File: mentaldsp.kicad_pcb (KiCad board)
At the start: 2 copper layers, 90 x 70 mm, 10 parts, among them J1 NEMA Conn, J2 NEMA Conn, J3 NEMA Conn, J4 NEMA Conn, U1 TMC2209_Node0, U2 ESP32-S3-DevKitC, U3 TMC2209_Node1, U4 TMC2209_Node2, U5 TMC2209_Node3

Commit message: basic routing
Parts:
- added J6: Barrel_Jack_Switch, lib_footprint:Generic_PowerJack, F.Cu at (84.5, 105.0)
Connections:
- U2 pad 10: /STEP2 -> /DIAG2
- U2 pad 11: /STEP3 -> unconnected-(U2-GPIO18/ADC2_CH7-Pad11)
- U2 pad 15: /DIAG0 -> /DIR1
- U2 pad 16: /DIAG1 -> /STEP1
- U2 pad 17: /DIAG2 -> /DIAG1
- U2 pad 18: /DIAG3 -> /DIR0
- U2 pad 19: unconnected-(U2-GPIO13/ADC2_CH2-Pad19) -> /STEP0
- U2 pad 20: unconnected-(U2-GPIO14/ADC2_CH3-Pad20) -> /DIAG0
- U2 pad 4: /DIR0 -> /DIR3
- U2 pad 5: /DIR1 -> /STEP3
- U2 pad 6: /DIR2 -> unconnected-(U2-GPIO6/ADC1_CH5-Pad6)
- U2 pad 7: /DIR3 -> /DIAG3
- U2 pad 8: /STEP0 -> /DIR2
- U2 pad 9: /STEP1 -> /STEP2
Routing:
- net +3.3V: track 0.00 -> 254.6 mm
- net /EN: track 0.00 -> 229.2 mm
- net /DIAG3: track 0.00 -> 83.0 mm
- net /DIAG1: track 0.00 -> 67.5 mm
- net /UART: track 4.58 -> 69.9 mm
- net /STEP3: track 0.00 -> 47.5 mm
- net /DIR3: track 0.00 -> 44.0 mm
- net /STEP1: track 0.00 -> 39.5 mm
- net /DIR1: track 0.00 -> 38.0 mm
- net /DIAG0: track 0.00 -> 21.7 mm
- net /STEP2: track 0.00 -> 20.1 mm
- net /DIR2: track 0.00 -> 19.9 mm
- net /DIAG2: track 0.00 -> 18.9 mm
- net GND: track 0.00 -> 14.8 mm
- net /DIR0: track 0.00 -> 9.87 mm
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
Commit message: v0.0.1 including power
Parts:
- moved J6 22.0 mm to (106.5, 104.6)
- moved R1 8.00 mm to (187.5, 79.0)
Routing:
- net GND: track 14.8 -> 249.3 mm
- net +12V: track 0.00 -> 115.9 mm
- net +3.3V: track 254.6 -> 300.6 mm
- net /EN: track 229.2 -> 224.9 mm
- net /DIAG3: track 83.0 -> 78.7 mm
- net /UART: track 69.9 -> 73.7 mm
- net Net-(U2-GPIO43/U0TXD): track 0.00 -> 3.66 mm
- added copper zone on B.Cu, net GND

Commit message: add uart via 1mm hole
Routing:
- net /UART: track 73.7 -> 152.8 mm, vias 0 -> 1
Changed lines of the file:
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@@
+	)
+	(segment
+		(start 187.5 80.6)
+		(end 187.5 85)
+		(width 0.4)
+		(layer "F.Cu")
+		(net 18)
+	)
+	(via
+		(at 187.5 85)
+		(size 1.5)
+		(drill 1)
+		(layers "F.Cu" "B.Cu")
+		(net 18)
+	)
+	(segment
+		(start 154.12 86.5)
+		(end 186 86.5)
+		(width 0.4)
+		(layer "B.Cu")
+		(net 18)
 	)
 	(segment
 		(start 144.876 130.744)
 		(end 153.85 121.77)
+		(width 0.4)
+		(layer "B.Cu")
+		(net 18)
+	)
+	(segment
+		(start 126.35 86.77)
+		(end 119.916 93.204)
 		(width 0.4)
 		(layer "B.Cu")
@@
 		(width 0.4)
 		(layer "B.Cu")
+		(net 18)
+	)
+	(segment
+		(start 186 86.5)
+		(end 187.5 85)
+		(width 0.4)
+		(layer "B.Cu")
+		(net 18)
+	)
+	(segment
+		(start 119.916 115.336)
+		(end 126.35 121.77)
+		(width 0.4)
+		(layer "B.Cu")
+		(net 18)
+	)
+	(segment
+		(start 119.916 93.204)
+		(end 119.916 115.336)
+		(width 0.4)
+		(layer "B.Cu")
+		(net 18)
+	)
+	(segment
+		(start 153.85 86.77)
+		(end 154.12 86.5)
+		(width 0.4)
+		(layer "B.Cu")

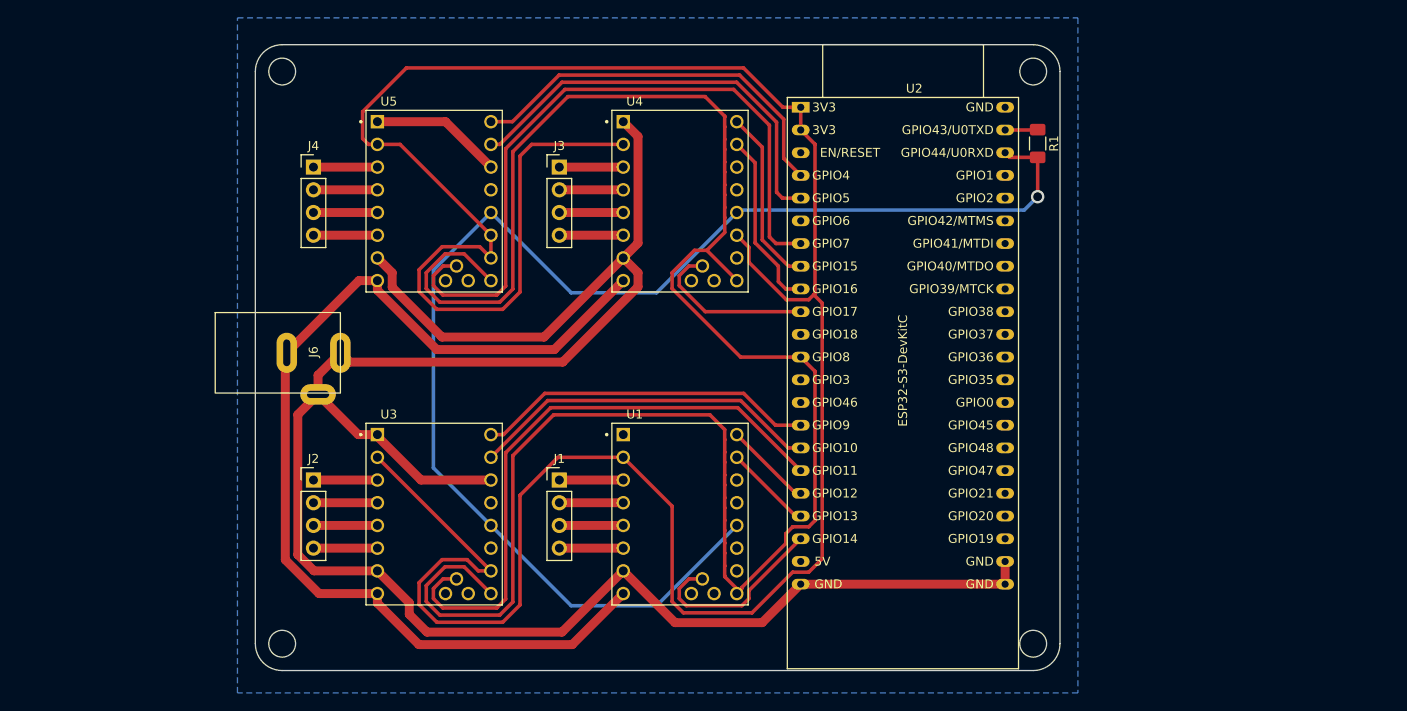
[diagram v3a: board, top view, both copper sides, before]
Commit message: v2 with BTT TMC2209
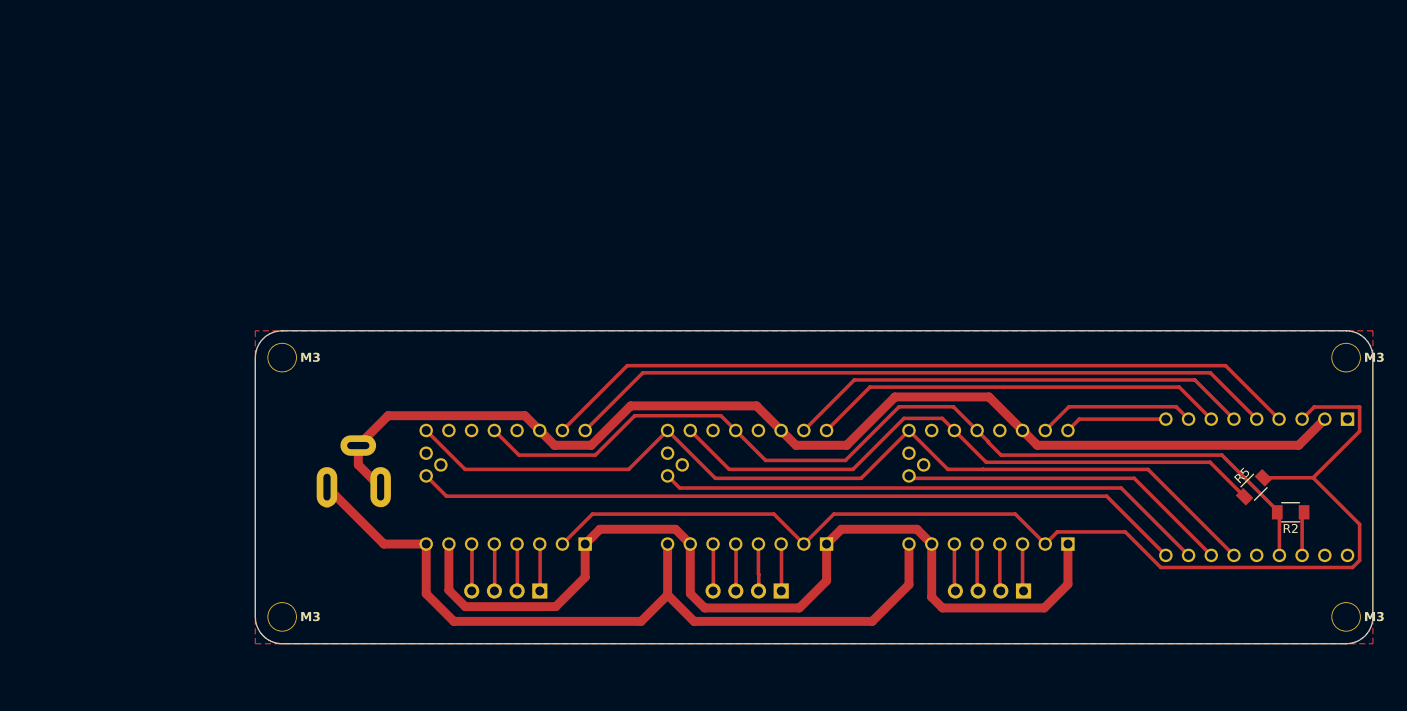
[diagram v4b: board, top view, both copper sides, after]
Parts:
- removed J1, J2, J3, J4: NEMA Conn, Connector_PinHeader_2.54mm:PinHeader_1x04_P2.54mm_Vertical
- removed J6: Barrel_Jack_Switch, lib_footprint:Generic_PowerJack
- removed R1: 1k, Resistor_SMD:R_1206_3216Metric_Pad1.30x1.75mm_HandSolder
- removed U1: TMC2209_Node0, footprints:MODULE_TMC2209_SILENTSTEPSTICK
- removed U2: ESP32-S3-DevKitC, PCM_Espressif:ESP32-S3-DevKitC
- removed U3: TMC2209_Node1, footprints:MODULE_TMC2209_SILENTSTEPSTICK
- removed U4: TMC2209_Node2, footprints:MODULE_TMC2209_SILENTSTEPSTICK
- removed U5: TMC2209_Node3, footprints:MODULE_TMC2209_SILENTSTEPSTICK
- added H1: ~, PCM_fab:MountingHole_M3, F.Cu at (222.0, 132.0)
- added H2: ~, PCM_fab:MountingHole_M3, F.Cu at (222.0, 103.0)
- added H3: ~, PCM_fab:MountingHole_M3, F.Cu at (103.0, 132.0)
- added H4: ~, PCM_fab:MountingHole_M3, F.Cu at (103.0, 103.0)
- added J5: NEMA Conn, Connector_PinHeader_2.54mm:PinHeader_1x04_P2.54mm_Vertical, B.Cu at (131.8, 129.1)
- added J7: NEMA Conn, Connector_PinHeader_2.54mm:PinHeader_1x04_P2.54mm_Vertical, B.Cu at (185.9, 129.1)
- added J8: NEMA Conn, Connector_PinHeader_2.54mm:PinHeader_1x04_P2.54mm_Vertical, B.Cu at (158.8, 129.1)
- added J9: Barrel_Jack_Switch, lib_footprint:Generic_PowerJack, B.Cu at (111.0, 115.3)
- added R2: 1k, PCM_fab:R_1206, F.Cu at (215.8, 120.3)
- added R5: 0, PCM_fab:R_1206, F.Cu at (211.7, 117.5)
- added U6: ESP32-S3-SUPERMINI, lib_footprint:ESP32-S3-SuperMini, B.Cu at (212.0, 117.5)
- added U7: TMC2209_N0, lib_footprint:BTT_TMC2209, B.Cu at (128.0, 117.5)
- added U8: TMC2209_N1, lib_footprint:BTT_TMC2209, B.Cu at (155.0, 117.5)
- added U9: TMC2209_N2, lib_footprint:BTT_TMC2209, B.Cu at (182.0, 117.5)
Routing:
- net /EN: track 224.9 -> 104.2 mm
- net +3.3V: track 300.6 -> 201.4 mm
- net /DIAG3: track 78.7 -> 0.00 mm
- net /STEP0: track 9.87 -> 85.6 mm
- net /DIR0: track 9.87 -> 79.9 mm
- net /DIAG0: track 21.7 -> 86.4 mm
- net /STEP3: track 47.5 -> 0.00 mm
- net /UART: track 152.8 -> 105.8 mm, vias 1 -> 0
- net /DIR3: track 44.0 -> 0.00 mm
- net +12V: track 115.9 -> 90.8 mm
- net /DIAG2: track 18.9 -> 37.5 mm
- net GND: track 249.3 -> 232.5 mm
- net /STEP1: track 39.5 -> 52.3 mm
- net /DIR1: track 38.0 -> 46.5 mm
- net /DIR2: track 19.9 -> 11.5 mm
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- added copper zone on F.Cu, net GND
- removed copper zone on B.Cu, net GND
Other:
- board size 90 x 70 mm -> 125 x 35 mm

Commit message: decoupling
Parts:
- added C1: 100n, PCM_fab:C_1206, F.Cu at (135.5, 126.5)
- added C10: 100n, PCM_fab:C_1206, F.Cu at (174.0, 126.5)
- added C11: 10u, PCM_fab:C_1206, F.Cu at (174.0, 129.0)
- added C12: 100n, PCM_fab:C_1206, F.Cu at (109.0, 108.5)
- added C13: 220u, PCM_fab:CP_Elec_100uF_Panasonic_EEE-FN1E101UL, F.Cu at (104.3, 110.3)
- added C2: 100n, PCM_fab:C_1206, F.Cu at (162.5, 126.5)
- added C3: 100n, PCM_fab:C_1206, F.Cu at (189.5, 126.5)
- added C4: 100n, PCM_fab:C_1206, F.Cu at (217.0, 114.3)
- added C5: 10u, PCM_fab:C_1206, F.Cu at (219.5, 114.3)
- added C6: 100n, PCM_fab:C_1206, F.Cu at (120.0, 126.5)
- added C7: 10u, PCM_fab:C_1206, F.Cu at (120.0, 129.0)
- added C8: 100n, PCM_fab:C_1206, F.Cu at (147.0, 126.5)
- added C9: 10u, PCM_fab:C_1206, F.Cu at (147.0, 129.0)
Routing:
- net GND: track 232.5 -> 246.5 mm
- net +12V: track 90.8 -> 102.0 mm
- net +3.3V: track 201.4 -> 210.8 mm

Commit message: cleanup
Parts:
- added R6: 10k, PCM_fab:R_1206, F.Cu at (207.5, 117.5)
- added R7: 0, PCM_fab:R_1206, F.Cu at (148.5, 107.5)
- added R8: 0, PCM_fab:R_1206, F.Cu at (178.0, 107.5)
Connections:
- U7 pad 14: unconnected-(U7-MS2-Pad14) -> GND
- U7 pad 15: unconnected-(U7-MS1-Pad15) -> GND
- U8 pad 14: unconnected-(U8-MS2-Pad14) -> +3.3V
- U8 pad 15: +3.3V -> GND
- U9 pad 14: +3.3V -> GND
- U9 pad 15: unconnected-(U9-MS1-Pad15) -> +3.3V
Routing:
- net GND: track 246.5 -> 257.8 mm
- net /UART: track 105.8 -> 109.4 mm
- net +3.3V: track 210.8 -> 208.3 mm
- net /EN: track 104.2 -> 106.4 mm
- net /DIR0: track 79.9 -> 81.3 mm
- net /STEP0: track 85.6 -> 87.0 mm
- net /DIR1: track 46.5 -> 47.8 mm
- net /STEP1: track 52.3 -> 53.6 mm

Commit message: cleanup2
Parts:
- U8: value TMC2209_N1 -> TMC2209_N2
- U9: value TMC2209_N2 -> TMC2209_N1
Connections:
- U6 pad 10: /DIR1 -> /DIR2
- U6 pad 11: /STEP1 -> /STEP2
- U6 pad 5: /DIAG2 -> /DIAG1
- U6 pad 6: /DIAG1 -> /DIAG2
- U6 pad 8: /DIR2 -> /DIR1
- U6 pad 9: /STEP2 -> /STEP1
- U8 pad 10: /STEP1 -> /STEP2
- U8 pad 18: /DIAG1 -> /DIAG2
- U8 pad 9: /DIR1 -> /DIR2
- U9 pad 10: /STEP2 -> /STEP1
- U9 pad 18: /DIAG2 -> /DIAG1
- U9 pad 9: /DIR2 -> /DIR1
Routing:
- net /DIR2: track 11.5 -> 47.8 mm
- net /DIR1: track 47.8 -> 11.5 mm
- net /STEP2: track 17.7 -> 53.6 mm
- net /STEP1: track 53.6 -> 17.7 mm
- net /DIAG2: track 37.5 -> 62.0 mm
- net /DIAG1: track 62.0 -> 37.5 mm

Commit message: gerber
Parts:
- C1, C10, C11, C12, C2, C3, C4, C5, C6, C7, C8, C9: footprint PCM_fab:C_1206 -> Capacitor_SMD:C_1206_3216Metric
- R2, R5, R6, R7, R8: footprint PCM_fab:R_1206 -> Resistor_SMD:R_1206_3216Metric
